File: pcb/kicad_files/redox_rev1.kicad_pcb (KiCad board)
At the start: 2 copper layers, 162.2 x 126.5 mm, 90 parts, among them K0 KEYSW, K1 KEYSW, K10 KEYSW, K11 KEYSW, K12 KEYSW, K13 KEYSW, K14 KEYSW, K15 KEYSW, K16 KEYSW, K2 KEYSW, K20 KEYSW, K21 KEYSW, K22 KEYSW, K23 KEYSW, K24 KEYSW, K25 KEYSW, K26 KEYSW, K3 KEYSW, K30 KEYSW, K31 KEYSW, K32 KEYSW, K33 KEYSW, K34 KEYSW, K35 KEYSW, K36 KEYSW, K4 KEYSW, K40 KEYSW, K41 KEYSW, K42 KEYSW, K43 KEYSW, K44 KEYSW, K45 KEYSW, K46 KEYSW, K5 KEYSW, K6 KEYSW, U1 ProMicro

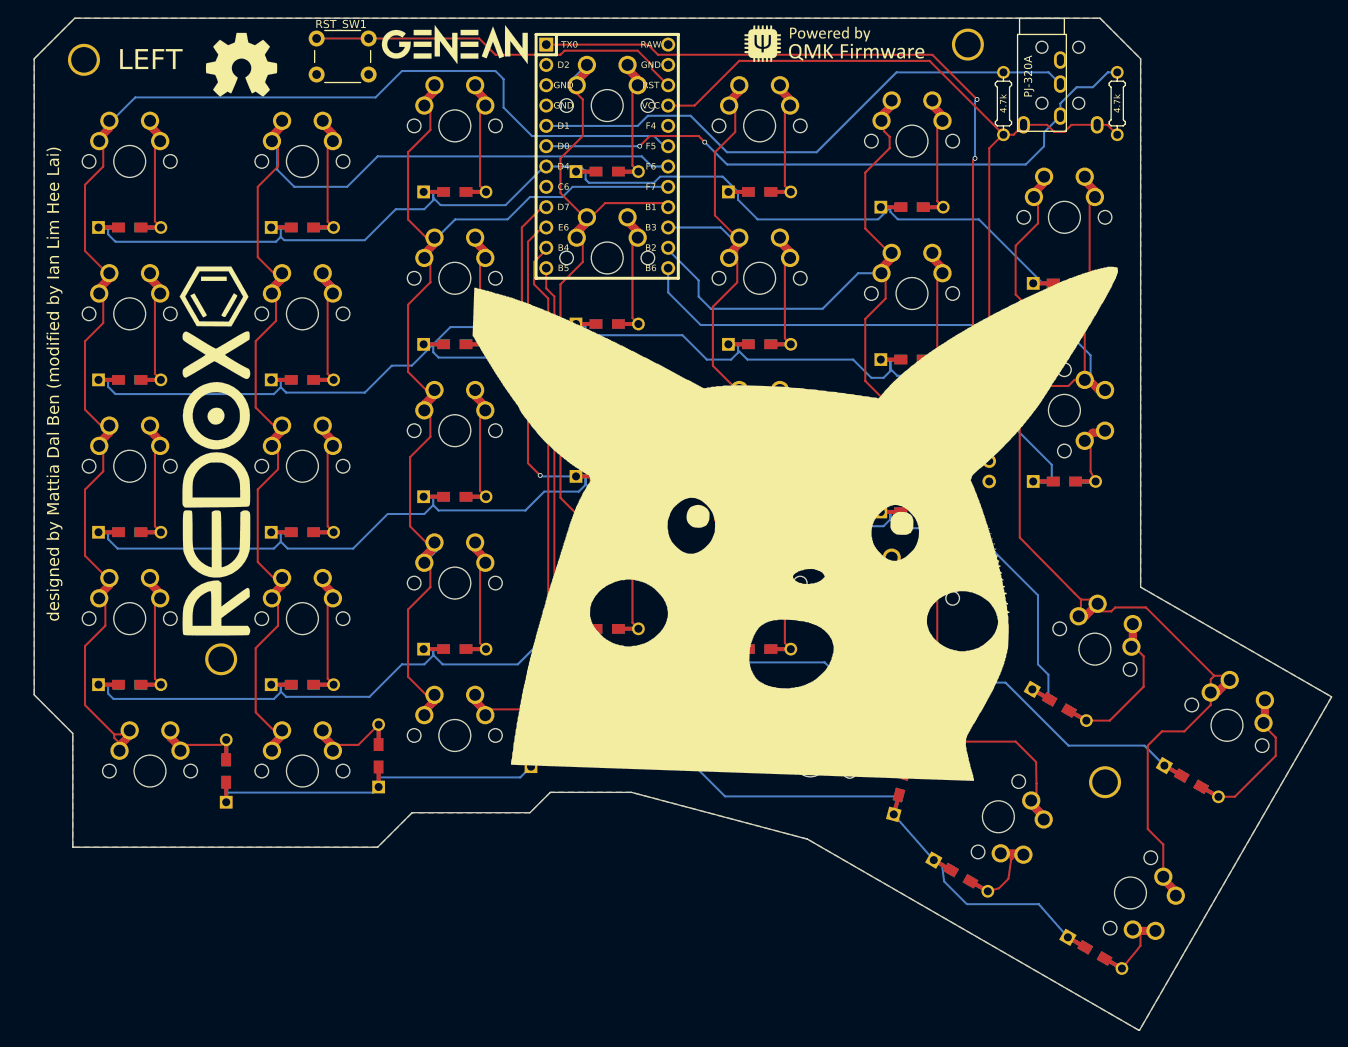
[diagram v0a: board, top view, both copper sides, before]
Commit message: included oled updates
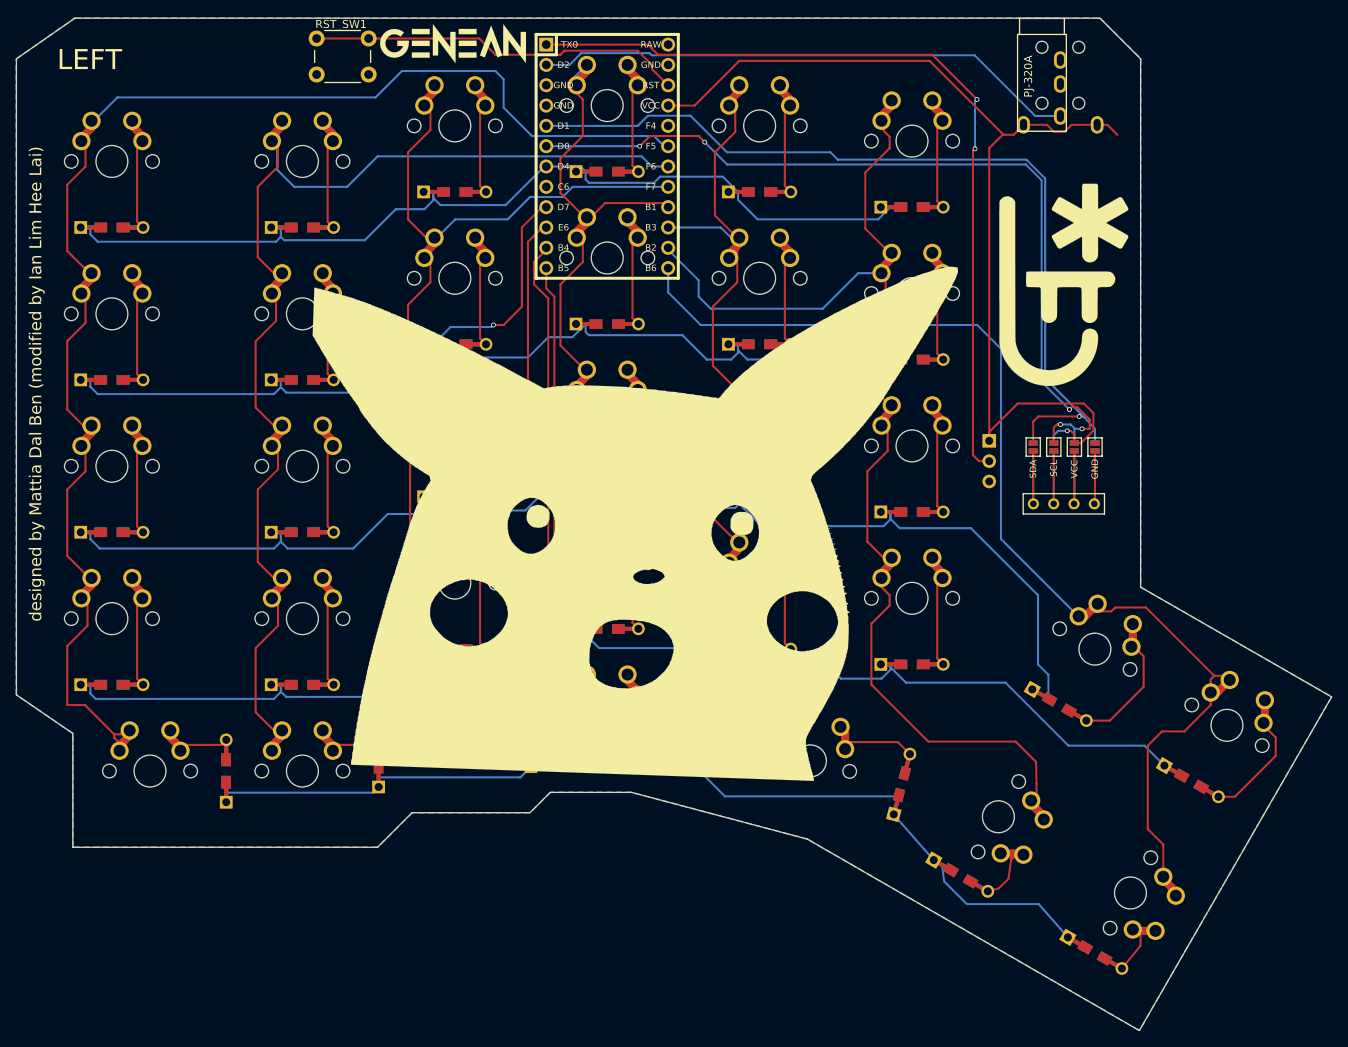
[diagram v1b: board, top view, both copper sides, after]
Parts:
- removed D16, D6: D, Keebio-Parts:Diode-dual
- removed the G*** at (132.3, 52.1)
- removed the G*** at (132.1, 52.1)
- removed the G*** at (102.2, 102.9)
- removed the G*** at (102.2, 102.2)
- removed the G*** at (179.6, 51.9)
- removed the G*** at (180.6, 51.9)
- removed HOLE_M3 (x4): VAL**, keyboard_parts:HOLE_M3
- removed K16, K6: KEYSW, keyswitches:SW_MX_reversible
- removed R1, R2: 4.7k, Keebio-Parts:Resistor-Compact
- removed REF*** (x2): OSHW-Logo2_14.6x12mm_SilkScreen, Symbols:OSHW-Symbol_8.9x8mm_SilkScreen
- added G***: LOGO, redox_footprints:genean-logo-fp, F.Cu at (131.8, 52.0)
- added G***: LOGO, redox_footprints:genean-logo-fp, B.Cu at (132.4, 51.9)
- added G***: LOGO, keyswitches:school_logo, B.Cu at (206.7, 82.1)
- added G***: LOGO, keyswitches:school_logo, F.Cu at (208.2, 82.1)
- added J1: OLED-Lily58-cache, Lily58_Pro-footprint:OLED_4Pin, F.Cu at (204.4, 109.5)
- added JP1: SDA, Lily58_Pro-footprint:Jumper, F.Cu at (204.4, 102.4)
- added JP2: SCL, Lily58_Pro-footprint:Jumper, F.Cu at (206.9, 102.4)
- added JP3: VCC, Lily58_Pro-footprint:Jumper, F.Cu at (209.5, 102.4)
- added JP4: GND, Lily58_Pro-footprint:Jumper, F.Cu at (212.1, 102.4)
- added JP5: GND, Lily58_Pro-footprint:Jumper, B.Cu at (204.4, 102.4)
- added JP6: VCC, Lily58_Pro-footprint:Jumper, B.Cu at (206.9, 102.4)
- added JP7: SCL, Lily58_Pro-footprint:Jumper, B.Cu at (209.5, 102.4)
- added JP8: SDA, Lily58_Pro-footprint:Jumper, B.Cu at (212.1, 102.4)
- moved G*** 20.0 mm to (159.8, 103.6)
- moved G*** 20.0 mm to (159.6, 103.6)
- moved D0 2.22 mm to (89.2, 74.9)
- moved D10 2.22 mm to (89.2, 94.0)
- moved D20 2.22 mm to (89.2, 113.0)
- moved D30 2.22 mm to (89.2, 132.1)
- moved K0 2.22 mm to (89.2, 66.7)
- moved K10 2.22 mm to (89.2, 85.7)
- moved K20 2.22 mm to (89.2, 104.8)
- moved K30 2.22 mm to (89.2, 123.8)
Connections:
- TRRS1 pad 2: SCL -> serial
- TRRS1 pad 3: SDA -> Net-(TRRS1-Pad3)
- U1 pad 2: Net-(U1-Pad2) -> serial
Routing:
- net serial: track 0.00 -> 68.1 mm
- net col6: track 203.5 -> 146.8 mm
- net SDA: track 71.4 -> 111.2 mm, vias 0 -> 1
- net SCL: track 80.1 -> 108.0 mm, vias 2 -> 5
- net VCC: track 103.1 -> 129.4 mm, vias 0 -> 1
- net row1: track 169.3 -> 144.3 mm
- net row0: track 135.3 -> 114.2 mm
- net Net-(D6-Pad2): track 14.9 -> 0.00 mm
- net Net-(J1-Pad4): track 0.00 -> 13.3 mm
- net Net-(J1-Pad3): track 0.00 -> 13.2 mm
- net Net-(J1-Pad1): track 0.00 -> 13.2 mm
- net Net-(J1-Pad2): track 0.00 -> 13.2 mm
- net Net-(D16-Pad2): track 9.20 -> 0.00 mm
- net col0: track 183.1 -> 187.6 mm
- net row2: track 188.9 -> 191.2 mm
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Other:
- board size 162.2 x 126.5 mm -> 164.4 x 126.5 mm

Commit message: Added gitignore
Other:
- net class Default removed
- net class PTH Connectors removed
